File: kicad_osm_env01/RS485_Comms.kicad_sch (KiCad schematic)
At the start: 17 parts, among them U7 ST3485EBDR

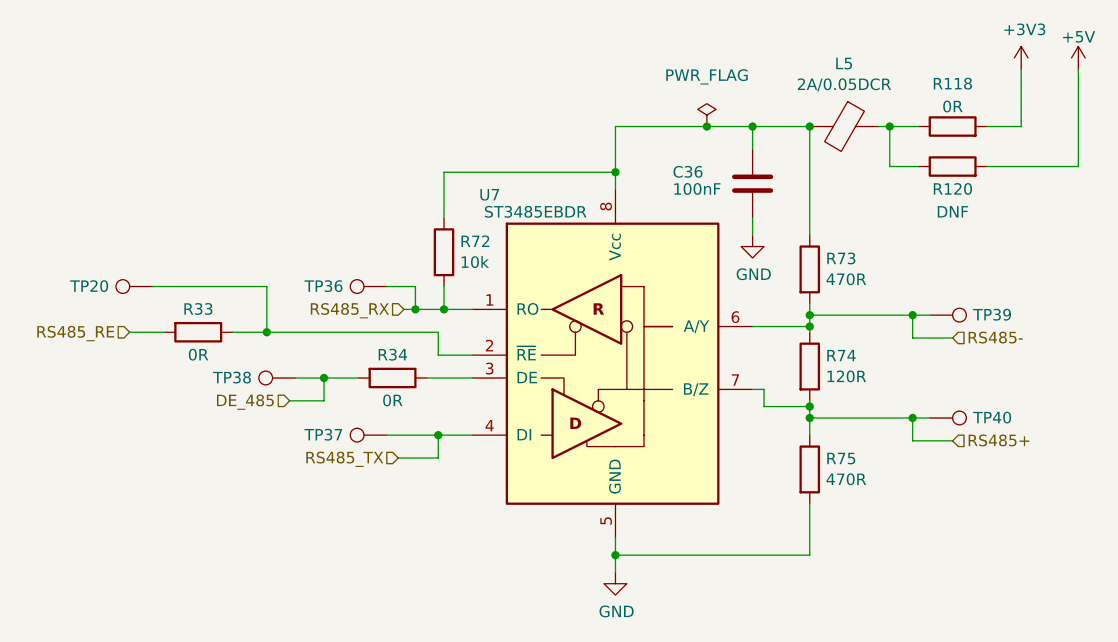
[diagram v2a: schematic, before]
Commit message: assigned all footprints
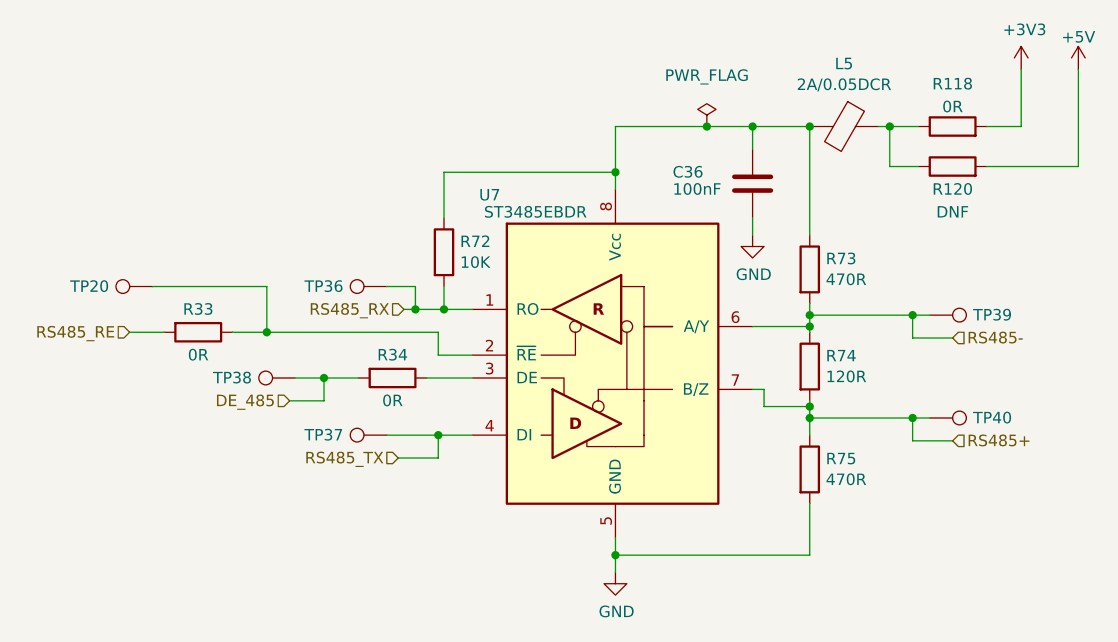
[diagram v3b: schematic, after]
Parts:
- C36: Voltage (none) -> 50V
- R118, R120, R33, R34: footprint Resistor_SMD:R_0603_1608Metric -> Resistor_SMD:R_0402_1005Metric
- R72: value 10k -> 10K; footprint Resistor_SMD:R_0603_1608Metric -> Resistor_SMD:R_0402_1005Metric
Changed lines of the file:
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@@
   (title_block
     (title "Open Smart Monitor")
-    (date "2022-09-26")
-    (rev "C")
+    (date "2023-09-29")
+    (rev "C.2")
     (company "Devtank LTD")
     (comment 1 "Part No: 304-010")
@@
       (effects (font (size 1.27 1.27)) hide)
     )
+    (property "Voltage" "50V" (at 158.75 78.105 0)
+      (effects (font (size 1.27 1.27)) hide)
+    )
     (pin "1")
     (pin "2")
@@
       (effects (font (size 1.27 1.27)) (justify left))
     )
-    (property "Value" "10k" (at 126.238 86.868 0)
-      (effects (font (size 1.27 1.27)) (justify left))
-    )
-    (property "Footprint" "Resistor_SMD:R_0603_1608Metric" (at 122.682 85.725 90)
+    (property "Value" "10K" (at 126.238 86.868 0)
+      (effects (font (size 1.27 1.27)) (justify left))
+    )
+    (property "Footprint" "Resistor_SMD:R_0402_1005Metric" (at 122.682 85.725 90)
       (effects (font (size 1.27 1.27)) hide)
     )
@@
       (effects (font (size 1.27 1.27)))
     )
-    (property "Footprint" "Resistor_SMD:R_0603_1608Metric" (at 118.745 97.917 90)
+    (property "Footprint" "Resistor_SMD:R_0402_1005Metric" (at 118.745 97.917 90)
       (effects (font (size 1.27 1.27)) hide)
     )
@@
       (effects (font (size 1.27 1.27)))
     )
-    (property "Footprint" "Resistor_SMD:R_0603_1608Metric" (at 97.155 92.837 90)
+    (property "Footprint" "Resistor_SMD:R_0402_1005Metric" (at 97.155 92.837 90)
       (effects (font (size 1.27 1.27)) hide)
     )
@@
       (effects (font (size 1.27 1.27)))
     )
-    (property "Footprint" "Resistor_SMD:R_0603_1608Metric" (at 180.975 77.978 90)
+    (property "Footprint" "Resistor_SMD:R_0402_1005Metric" (at 180.975 77.978 90)
       (effects (font (size 1.27 1.27)) hide)
     )
@@
       (effects (font (size 1.27 1.27)))
     )
-    (property "Footprint" "Resistor_SMD:R_0603_1608Metric" (at 180.975 73.533 90)
-      (effects (font (size 1.27 1.27)) hide)
-    )
+    (property "Footprint" "Resistor_SMD:R_0402_1005Metric" (at 180.975 73.533 90)
+      (effects (font (size 1.27 1.27)) hide)
+    )

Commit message: added tracking to layout
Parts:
- TP20, TP36, TP37, TP38, TP39, TP40: footprint TestPoint:TestPoint_THTPad_D1.0mm_Drill0.5mm -> TestPoint:TestPoint_Pad_D1.5mm
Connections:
- net RS485_RE: now also TP20.1
- net at R33.1, U7.2 (~{RE}): no longer TP20.1
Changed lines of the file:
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@@
   (junction (at 143.51 76.835) (diameter 0) (color 0 0 0 0)
   )
+  (junction (at 92.71 94.615) (diameter 0) (color 0 0 0 0)
+  )
   (junction (at 165.1 71.755) (diameter 0) (color 0 0 0 0)
   )
@@
   (junction (at 111.125 99.695) (diameter 0) (color 0 0 0 0)
   )
-  (junction (at 104.775 94.615) (diameter 0) (color 0 0 0 0)
-  )
   (junction (at 165.1 92.71) (diameter 0) (color 0 0 0 0)
   )
@@
     (stroke (width 0) (type default))
   )
-  (wire (pts (xy 104.775 89.535) (xy 104.775 94.615))
-    (stroke (width 0) (type default))
-  )
   (wire (pts (xy 118.11 89.535) (xy 121.285 89.535))
     (stroke (width 0) (type default))
@@
     (stroke (width 0) (type default))
   )
-  (wire (pts (xy 92.075 89.535) (xy 104.775 89.535))
-    (stroke (width 0) (type default))
-  )
   (wire (pts (xy 120.015 92.075) (xy 121.285 92.075))
     (stroke (width 0) (type default))
   )
-  (wire (pts (xy 100.965 94.615) (xy 104.775 94.615))
+  (wire (pts (xy 100.965 94.615) (xy 123.825 94.615))
     (stroke (width 0) (type default))
   )
@@
     (stroke (width 0) (type default))
   )
+  (wire (pts (xy 92.71 89.535) (xy 92.71 94.615))
+    (stroke (width 0) (type default))
+  )
   (wire (pts (xy 160.02 102.87) (xy 165.1 102.87))
     (stroke (width 0) (type default))
@@
     (stroke (width 0) (type default))
   )
+  (wire (pts (xy 92.71 94.615) (xy 89.535 94.615))
+    (stroke (width 0) (type default))
+  )
   (wire (pts (xy 176.53 104.14) (xy 178.435 104.14))
     (stroke (width 0) (type default))
@@
     (stroke (width 0) (type default))
   )
+  (wire (pts (xy 92.075 89.535) (xy 92.71 89.535))
+    (stroke (width 0) (type default))
+  )
   (wire (pts (xy 143.51 71.755) (xy 153.67 71.755))
     (stroke (width 0) (type default))
@@
     (stroke (width 0) (type default))
   )
-  (wire (pts (xy 93.345 94.615) (xy 89.535 94.615))
+  (wire (pts (xy 93.345 94.615) (xy 92.71 94.615))
     (stroke (width 0) (type default))
   )
   (wire (pts (xy 118.11 106.045) (xy 123.825 106.045))
-    (stroke (width 0) (type default))
-  )
-  (wire (pts (xy 104.775 94.615) (xy 123.825 94.615))
     (stroke (width 0) (type default))
   )
@@
       (effects (font (size 1.27 1.27)) hide)
     )
-    (property "Footprint" "TestPoint:TestPoint_THTPad_D1.0mm_Drill0.5mm" (at 178.435 97.79 0)
+    (property "Footprint" "TestPoint:TestPoint_Pad_D1.5mm" (at 178.435 97.79 0)
       (effects (font (size 1.27 1.27)) hide)
     )
@@
       (effects (font (size 1.27 1.27)) hide)
     )
-    (property "Footprint" "TestPoint:TestPoint_THTPad_D1.0mm_Drill0.5mm" (at 178.435 109.22 0)
+    (property "Footprint" "TestPoint:TestPoint_Pad_D1.5mm" (at 178.435 109.22 0)
       (effects (font (size 1.27 1.27)) hide)
     )
@@
       (effects (font (size 1.27 1.27)) hide)
     )
-    (property "Footprint" "TestPoint:TestPoint_THTPad_D1.0mm_Drill0.5mm" (at 107.95 94.615 0)
+    (property "Footprint" "TestPoint:TestPoint_Pad_D1.5mm" (at 107.95 94.615 0)
       (effects (font (size 1.27 1.27)) hide)
     )
@@
       (effects (font (size 1.27 1.27)) hide)
     )
-    (property "Footprint" "TestPoint:TestPoint_THTPad_D1.0mm_Drill0.5mm" (at 118.11 100.965 0)
+    (property "Footprint" "TestPoint:TestPoint_Pad_D1.5mm" (at 118.11 100.965 0)
       (effects (font (size 1.27 1.27)) hide)
     )
@@
       (effects (font (size 1.27 1.27)) hide)
     )
-    (property "Footprint" "TestPoint:TestPoint_THTPad_D1.0mm_Drill0.5mm" (at 118.11 84.455 0)
+    (property "Footprint" "TestPoint:TestPoint_Pad_D1.5mm" (at 118.11 84.455 0)
       (effects (font (size 1.27 1.27)) hide)
     )
@@
       (effects (font (size 1.27 1.27)) hide)
     )
-    (property "Footprint" "TestPoint:TestPoint_THTPad_D1.0mm_Drill0.5mm" (at 92.075 84.455 0)
-      (effects (font (size 1.27 1.27)) hide)
-    )
+    (property "Footprint" "TestPoint:TestPoint_Pad_D1.5mm" (at 92.075 84.455 0)
+      (effects (font (size 1.27 1.27)) hide)
+    )

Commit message: added information to symbol entries table, added jumper settings table, minor single track update on layout
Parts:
- C36: Characteristics (none) -> X5R; Other (none) -> Can use own part, but needs to meet the specs
- L5: Manufacturer (none) -> TDK; Manufacturer Part Number (none) -> MPZ1005S121HT000; Other (none) -> Can use own part, but needs to meet the specs
- R118, R120, R33, R34, R72, R73, R74, R75: Tolerance (none) -> 1%
- U7: Manufacturer (none) -> STMicroelectronics; Manufacturer Part Number (none) -> ST3485EBDR
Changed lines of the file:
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@@
       (effects (font (size 1.27 1.27) italic) hide)
     )
-    (property "Datasheet" "http://www.intersil.com/content/dam/Intersil/documents/isl8/isl83483-85-88-90-91.pdf" (at 140.335 99.695 0)
+    (property "Datasheet" "http://www.intersil.com/content/dam/Intersil/documents/isl8/isl83483-85-88-90-91.https://www.mouser.co.uk/datasheet/2/389/st3485eb-1850066.pdf" (at 140.335 99.695 0)
+      (effects (font (size 1.27 1.27)) hide)
+    )
+    (property "Manufacturer" "STMicroelectronics " (at 143.51 99.695 0)
+      (effects (font (size 1.27 1.27)) hide)
+    )
+    (property "Manufacturer Part Number" "ST3485EBDR" (at 143.51 99.695 0)
+      (effects (font (size 1.27 1.27)) hide)
+    )
+    (property "Power Rating" "" (at 143.51 99.695 0)
+      (effects (font (size 1.27 1.27)) hide)
+    )
+    (property "Current Rating" "" (at 143.51 99.695 0)
       (effects (font (size 1.27 1.27)) hide)
     )
@@
       (effects (font (size 1.27 1.27)) hide)
     )
+    (property "Power Rating" "" (at 158.75 78.105 0)
+      (effects (font (size 1.27 1.27)) hide)
+    )
+    (property "Characteristics" "X5R" (at 158.75 78.105 0)
+      (effects (font (size 1.27 1.27)) hide)
+    )
+    (property "Current Rating" "" (at 158.75 78.105 0)
+      (effects (font (size 1.27 1.27)) hide)
+    )
+    (property "Other" "Can use own part, but needs to meet the specs" (at 158.75 78.105 0)
+      (effects (font (size 1.27 1.27)) hide)
+    )
     (pin "1")
     (pin "2")
@@
       (effects (font (size 1.27 1.27)) hide)
     )
+    (property "Tolerance" "1%" (at 124.46 85.725 0)
+      (effects (font (size 1.27 1.27)) hide)
+    )
+    (property "Power Rating" "" (at 124.46 85.725 0)
+      (effects (font (size 1.27 1.27)) hide)
+    )
+    (property "Current Rating" "" (at 124.46 85.725 0)
+      (effects (font (size 1.27 1.27)) hide)
+    )
     (pin "1")
     (pin "2")
@@
       (effects (font (size 1.27 1.27)) hide)
     )
+    (property "Tolerance" "1%" (at 165.1 87.63 0)
+      (effects (font (size 1.27 1.27)) hide)
+    )
+    (property "Power Rating" "" (at 165.1 87.63 0)
+      (effects (font (size 1.27 1.27)) hide)
+    )
+    (property "Current Rating" "" (at 165.1 87.63 0)
+      (effects (font (size 1.27 1.27)) hide)
+    )
     (pin "1")
     (pin "2")
@@
       (effects (font (size 1.27 1.27)) hide)
     )
+    (property "Tolerance" "1%" (at 165.1 98.425 0)
+      (effects (font (size 1.27 1.27)) hide)
+    )
+    (property "Power Rating" "" (at 165.1 98.425 0)
+      (effects (font (size 1.27 1.27)) hide)
+    )
+    (property "Current Rating" "" (at 165.1 98.425 0)
+      (effects (font (size 1.27 1.27)) hide)
+    )
     (pin "1")
     (pin "2")
@@
     )
     (property "Datasheet" "" (at 165.1 109.855 0)
+      (effects (font (size 1.27 1.27)) hide)
+    )
+    (property "Tolerance" "1%" (at 165.1 109.855 0)
+      (effects (font (size 1.27 1.27)) hide)
+    )
+    (property "Power Rating" "" (at 165.1 109.855 0)
+      (effects (font (size 1.27 1.27)) hide)
+    )
+    (property "Current Rating" "" (at 165.1 109.855 0)
       (effects (font (size 1.27 1.27)) hide)
     )
@@
       (effects (font (size 1.27 1.27)) hide)
     )
-    (property "Datasheet" "~" (at 178.435 97.79 0)
+    (property "Datasheet" "" (at 178.435 97.79 0)
+      (effects (font (size 1.27 1.27)) hide)
+    )
+    (property "Power Rating" "" (at 178.435 92.71 0)
+      (effects (font (size 1.27 1.27)) hide)
+    )
+    (property "Current Rating" "" (at 178.435 92.71 0)
       (effects (font (size 1.27 1.27)) hide)
     )
@@
       (effects (font (size 1.27 1.27)) hide)
     )
-    (property "Datasheet" "~" (at 178.435 109.22 0)
+    (property "Datasheet" "" (at 178.435 109.22 0)
+      (effects (font (size 1.27 1.27)) hide)
+    )
+    (property "Power Rating" "" (at 178.435 104.14 0)
+      (effects (font (size 1.27 1.27)) hide)
+    )
+    (property "Current Rating" "" (at 178.435 104.14 0)
       (effects (font (size 1.27 1.27)) hide)
     )
@@
       (effects (font (size 1.27 1.27)) hide)
     )
-    (property "Datasheet" "~" (at 107.95 94.615 0)
+    (property "Datasheet" "" (at 107.95 94.615 0)
+      (effects (font (size 1.27 1.27)) hide)
+    )
+    (property "Power Rating" "" (at 107.95 99.695 0)
+      (effects (font (size 1.27 1.27)) hide)
+    )
+    (property "Current Rating" "" (at 107.95 99.695 0)
       (effects (font (size 1.27 1.27)) hide)
     )
@@
       (effects (font (size 1.27 1.27)) hide)
     )
-    (property "Datasheet" "~" (at 118.11 100.965 0)
+    (property "Datasheet" "" (at 118.11 100.965 0)
+      (effects (font (size 1.27 1.27)) hide)
+    )
+    (property "Power Rating" "" (at 118.11 106.045 0)
+      (effects (font (size 1.27 1.27)) hide)
+    )
+    (property "Current Rating" "" (at 118.11 106.045 0)
       (effects (font (size 1.27 1.27)) hide)
     )
@@
       (effects (font (size 1.27 1.27)) hide)
     )
-    (property "Datasheet" "~" (at 118.11 84.455 0)
+    (property "Datasheet" "" (at 118.11 84.455 0)
+      (effects (font (size 1.27 1.27)) hide)
+    )
+    (property "Power Rating" "" (at 118.11 89.535 0)
+      (effects (font (size 1.27 1.27)) hide)
+    )
+    (property "Current Rating" "" (at 118.11 89.535 0)
       (effects (font (size 1.27 1.27)) hide)
     )
@@
       (effects (font (size 1.27 1.27)) hide)
     )
+    (property "Tolerance" "1%" (at 118.745 99.695 0)
+      (effects (font (size 1.27 1.27)) hide)
+    )
+    (property "Power Rating" "" (at 118.745 99.695 0)
+      (effects (font (size 1.27 1.27)) hide)
+    )
+    (property "Current Rating" "" (at 118.745 99.695 0)
+      (effects (font (size 1.27 1.27)) hide)
+    )
     (pin "1")
     (pin "2")
@@
       (effects (font (size 1.27 1.27)) hide)
     )
+    (property "Tolerance" "1%" (at 97.155 94.615 0)
+      (effects (font (size 1.27 1.27)) hide)
+    )
+    (property "Power Rating" "" (at 97.155 94.615 0)
+      (effects (font (size 1.27 1.27)) hide)
+    )
+    (property "Current Rating" "" (at 97.155 94.615 0)
+      (effects (font (size 1.27 1.27)) hide)
+    )
     (pin "1")
     (pin "2")
@@
     )
     (property "Datasheet" "" (at 168.91 71.755 0)
+      (effects (font (size 1.27 1.27)) hide)
+    )
+    (property "Manufacturer" "TDK" (at 168.91 71.755 0)
+      (effects (font (size 1.27 1.27)) hide)
+    )
+    (property "Manufacturer Part Number" "MPZ1005S121HT000 " (at 168.91 71.755 0)
+      (effects (font (size 1.27 1.27)) hide)
+    )
+    (property "Power Rating" "" (at 168.91 71.755 0)
+      (effects (font (size 1.27 1.27)) hide)
+    )
+    (property "Current Rating" "" (at 168.91 71.755 0)
+      (effects (font (size 1.27 1.27)) hide)
+    )
+    (property "Other" "Can use own part, but needs to meet the specs" (at 168.91 71.755 0)
       (effects (font (size 1.27 1.27)) hide)
     )
@@
       (effects (font (size 1.27 1.27)) hide)
     )
-    (property "Datasheet" "~" (at 92.075 84.455 0)
+    (property "Datasheet" "" (at 92.075 84.455 0)
+      (effects (font (size 1.27 1.27)) hide)
+    )
+    (property "Power Rating" "" (at 92.075 89.535 0)
+      (effects (font (size 1.27 1.27)) hide)
+    )
+    (property "Current Rating" "" (at 92.075 89.535 0)
       (effects (font (size 1.27 1.27)) hide)
     )
@@
     )
     (property "Datasheet" "" (at 180.975 76.2 0)
+      (effects (font (size 1.27 1.27)) hide)
+    )
+    (property "Tolerance" "1%" (at 180.975 76.2 0)
+      (effects (font (size 1.27 1.27)) hide)
+    )
+    (property "Power Rating" "" (at 180.975 76.2 0)
+      (effects (font (size 1.27 1.27)) hide)
+    )
+    (property "Current Rating" "" (at 180.975 76.2 0)
       (effects (font (size 1.27 1.27)) hide)
     )
@@
       (effects (font (size 1.27 1.27)) hide)
     )
+    (property "Tolerance" "1%" (at 180.975 71.755 0)
+      (effects (font (size 1.27 1.27)) hide)
+    )
+    (property "Power Rating" "" (at 180.975 71.755 0)
+      (effects (font (size 1.27 1.27)) hide)
+    )
+    (property "Current Rating" "" (at 180.975 71.755 0)
+      (effects (font (size 1.27 1.27)) hide)
+    )
